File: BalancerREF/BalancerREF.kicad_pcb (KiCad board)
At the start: 2 copper layers, 69.8 x 54 mm, 101 parts, among them J1 USB4105-GF-A, J2 LiPo 500mAh PROTECTED, J3 MAG+ / MAG- PTH, J4 GPS MODULE 3V3 UART, Q1 AO3400A, Q3 AO3401A, Q4 AO3401A, SW1 POWER, SW2 ACQUIRE, SW3 BOOT / SERVICE, SW4 RESET, U1 ESP32-S3-MINI-1-N8, U10 SN74LVC1G123DCTR, U2 IIS3DWBTR, U3 LM1815MX/NOPB, U4 TS3021IYLT, U5 MCP73831T-2ACI/OT, U6 TPS63031DSKR, U7 SRV05-4MR6T1G, U8 TLV9062IDR, U9 SN74LVC1G08DBVR

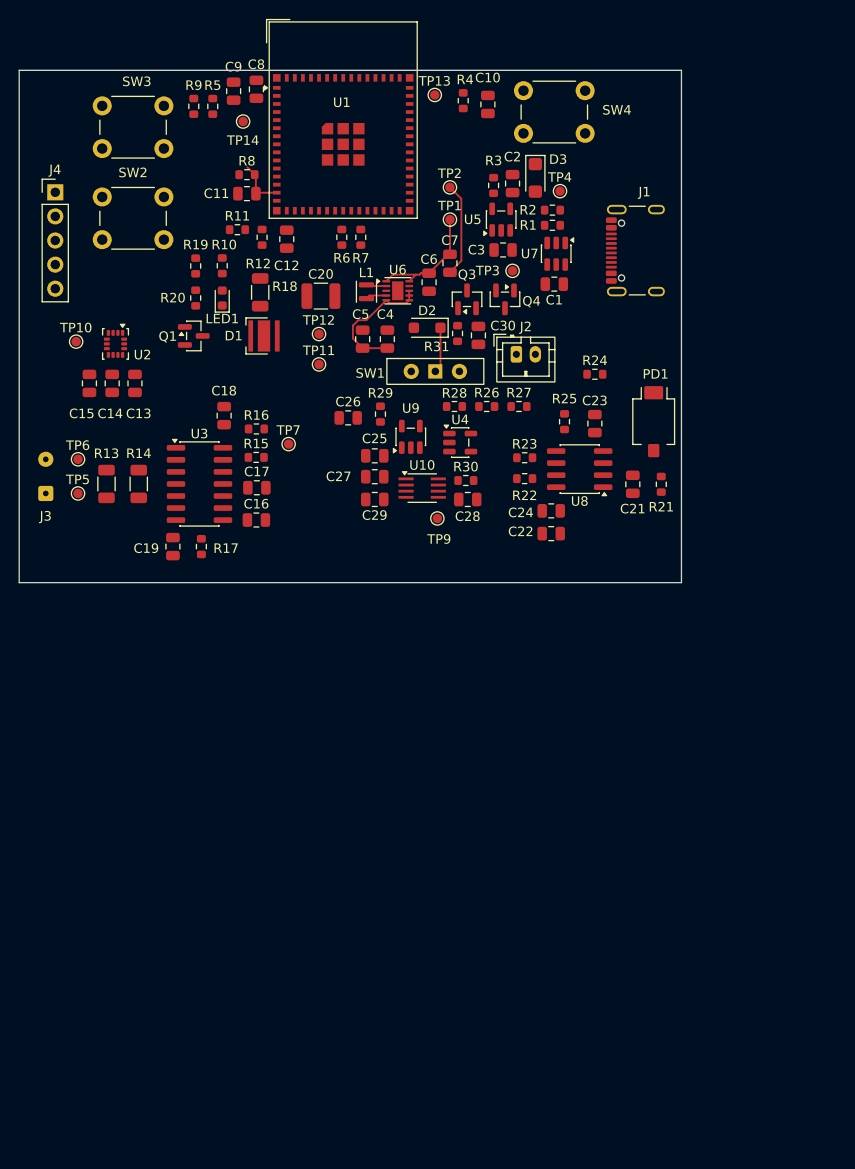
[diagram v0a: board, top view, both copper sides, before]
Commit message: feat: split optical head to its own board, place both PCBs
BalancerREF main board (50 x 50, 4 layer):
- optical front end removed to BalancerREF_OptHead; J5 7-way cable connector
  added, with ground interleaved between OPT_LED_EN and OPT_COMP
- SW4 (RESET) removed - SW1 feeds U6 VIN and EN, so the power slide already
  power-cycles the MCU; R4/C10/TP13 still hold EN high and probeable
- R5 removed - it duplicated R9's 10k BOOT pull-up on the same net
- all 83 footprints placed: ICs, connectors, switches and test points on the
  front, passives on the back under their own IC's power pins
- M2.5 mounting holes at the four corners
- UP / LEFT orientation markers on F.SilkS for vertical mounting with the
  ESP32 left and USB-C right
- DRC 2, both the U1 library courtyard overlapping the corner holes; U1's real
  antenna keepout is off-board thanks to the overhang

BalancerREF_OptHead (25 x 50, 2 layer), new PCB:
- every part on the front so B.Cu is an uninterrupted GND pour, which matters
  more than a clean optical face given the transimpedance summing node
- D1 centred on the optical axis, PD1 18 mm directly below, J5 on the bottom
- DRC 0

Verification:
- verify_netlist.py spec updated for the split and re-passing honestly. It had
  been reporting PASS against a stale netlist; regenerating that netlist made it
  crash, which is what the spec update fixes. PASS: 43 exact circuit nets,
  280 pin endpoints, 128 IC pads
- verify_head.py unchanged, PASS: 16 exact circuit nets, 63 pin endpoints
- review/ artifacts regenerated from the current schematic

Lens keepout radius and the D1-PD1 spacing are estimates pending the real
Ledil TINA holder dimensions.

Co-Authored-By: Claude Opus 5 (1M context) <noreply@anthropic.com>
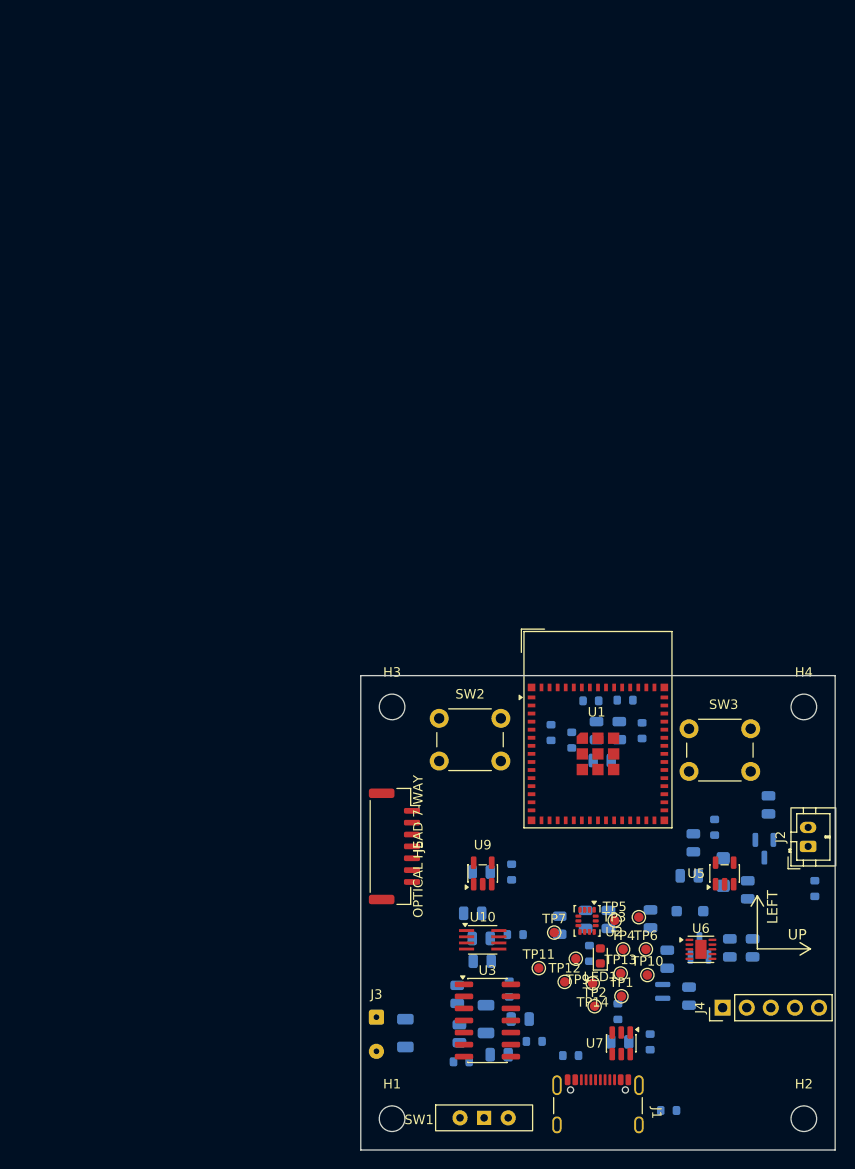
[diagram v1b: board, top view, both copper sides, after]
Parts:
- removed C20: 100u / 6.3V, Capacitor_SMD:C_1210_3225Metric
- removed C21: 10p C0G, Capacitor_SMD:C_0805_2012Metric
- removed C22: 10n, Capacitor_SMD:C_0805_2012Metric
- removed C23, C24, C25: 100n, Capacitor_SMD:C_0805_2012Metric
- removed D1: XPEBRD-L1 625nm, LED_SMD:LED_Cree-XP
- removed PD1: BPW34S, OptoDevice:Osram_BPW34S-SMD
- removed Q1: AO3400A, Package_TO_SOT_SMD:SOT-23
- removed R18: 3R0 1206 0.5W, Resistor_SMD:R_1206_3216Metric
- removed R19: 100R, Resistor_SMD:R_0603_1608Metric
- removed R20: 100k, Resistor_SMD:R_0603_1608Metric
- removed R21, R22, R24, R25, R27, R5: 10k, Resistor_SMD:R_0603_1608Metric
- removed R23: 120k, Resistor_SMD:R_0603_1608Metric
- removed R26: 22k, Resistor_SMD:R_0603_1608Metric
- removed R28: 470k, Resistor_SMD:R_0603_1608Metric
- removed SW4: RESET, Button_Switch_THT:SW_PUSH_6mm
- removed U4: TS3021IYLT, Package_TO_SOT_SMD:SOT-23-5
- removed U8: TLV9062IDR, Package_SO:SOIC-8_3.9x4.9mm_P1.27mm
- added H1: M2.5 MOUNT, MountingHole_2.7mm_M2.5, F.Cu at (103.3, 146.7)
- added H2: M2.5 MOUNT, MountingHole_2.7mm_M2.5, F.Cu at (146.7, 146.7)
- added H3: M2.5 MOUNT, MountingHole_2.7mm_M2.5, F.Cu at (103.3, 103.3)
- added H4: M2.5 MOUNT, MountingHole_2.7mm_M2.5, F.Cu at (146.7, 103.3)
- added J5: OPTICAL HEAD 7-WAY, Connector_JST:JST_GH_SM07B-GHS-TB_1x07-1MP_P1.25mm_Horizontal, F.Cu at (103.5, 118.0)
- C1, C10, C11, C12, C13, C14, C15, C16, C17, C18, C19, C2, C26, C27, C28, C29, C3, C30, C4, C5, C6, C7, C8, C9, D2, D3, L1, Q3, Q4, R1, R10, R11, R12, R13, R14, R15, R16, R17, R2, R29, R3, R30, R31, R4, R6, R7, R8, R9: moved to B.Cu
- moved J4 111.1 mm to (138.1, 135.0), turned to 90 degrees
- moved TP14 98.0 mm to (124.4, 132.4)
- moved TP13 94.6 mm to (127.4, 131.4)
- moved R1 94.1 mm to (132.4, 145.8), turned to 180 degrees
- moved J1 91.2 mm to (125.0, 146.3), turned to 0 degrees
- moved SW3 90.2 mm to (141.1, 110.1)
- moved R7 90.1 mm to (130.5, 138.6)
- moved TP10 89.9 mm to (130.2, 131.6)
- moved R2 89.1 mm to (122.1, 140.0), turned to 180 degrees
- moved C12 88.1 mm to (138.9, 128.7)
- moved TP2 87.6 mm to (124.7, 134.8)
- moved R6 86.6 mm to (127.1, 135.4)
- moved TP1 83.8 mm to (127.5, 133.8)
- moved U7 83.5 mm to (127.5, 138.8)
- moved R10 82.2 mm to (124.1, 129.3)
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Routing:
- net /SYS_SW: track 13.7 -> 0.00 mm
- net /+3V3: track 12.5 -> 0.00 mm
- net GND: track 9.94 -> 0.00 mm
- net /ACQUIRE_BUTTON: track 5.39 -> 0.00 mm
- net Net-(D2-K): track 4.82 -> 0.00 mm
- net Net-(U6-L1): track 2.22 -> 0.00 mm
- net Net-(U6-L2): track 2.14 -> 0.00 mm
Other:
- board size 69.8 x 54 mm -> 50 x 50 mm
- copper layers 2 -> 4
- board text added: "LEFT"
- board text added: "UP"

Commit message: feat: fiducials, net classes, and a BAT sense divider
Fiducials (1 mm dot / 2 mm mask), three per populated face at three of the
four corners - never four, since a symmetric set gives the placement machine
no way to distinguish a 180-degree-rotated panel. Main board gets both faces
(FID1-3 front, FID4-6 back); the optical head is single-sided so its back has
none.

Net classes set in both .kicad_pro, sized from IPC-2221 at 1 oz outer copper
and a 10 C rise (0.20 mm ~ 0.74 A, 0.50 ~ 1.45 A, 0.80 ~ 2.03 A):
  Default 0.20  Power 0.50  Switch 0.80 (main)  Emitter 0.80 (head)  USB pair
Switch clearance stays at 0.20 rather than 0.25: the TPS63031's WSON-10 puts
its own L1/L2 pads 0.20 mm from its thermal pad, so anything stricter fails
inside the package. The USB class exists for tuning and length matching but is
not an impedance solution - that needs the fab's stackup. The S3's native USB
is Full Speed, so it matters less than it would at High Speed.

BAT sense divider - R33/R34 (1M) and C31 (100n) on GPIO4 (ADC1_CH3):
SUPPLY_SENSE reads SYS_SW/2 and cannot separate USB from battery, because a
USB port at the low end of spec minus D2's drop lands near 4.30 V against a
full cell at 4.20 V - inside divider tolerance plus ADC error. Comparing
SYS_SW against BAT is a differential test and separates them cleanly. 1M/1M
rather than 100k/100k because this divider hangs on the cell even when the
puck is off (~2 uA vs ~21 uA); the resulting 500k source impedance means
firmware needs a long sample time and multisample.

U1 pin 8's no-connect removed and U1.8 dropped from unused-pins.json.

verify_netlist.py spec extended with BAT_SENSE and the new ground/BAT members.
  main PASS: 44 exact circuit nets, 286 pin endpoints, 128 IC pads
  head PASS: 16 exact circuit nets, 63 pin endpoints
ERC 0 errors. DRC: main 2 (U1 library courtyard vs the corner holes), head 0.
All 81 schematic parts confirmed present on the board; the only board-only
refs are the 6 fiducials and 4 mounting hole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
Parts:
- added C31: 100n, C_0805_2012Metric, B.Cu at (121.3, 111.4)
- added FID1: FIDUCIAL, Fiducial_1mm_Mask2mm, F.Cu at (141.5, 146.5)
- added FID2: FIDUCIAL, Fiducial_1mm_Mask2mm, F.Cu at (103.5, 127.0)
- added FID3: FIDUCIAL, Fiducial_1mm_Mask2mm, F.Cu at (142.5, 118.5)
- added FID4: FIDUCIAL, Fiducial_1mm_Mask2mm, B.Cu at (143.0, 146.5)
- added FID5: FIDUCIAL, Fiducial_1mm_Mask2mm, B.Cu at (103.5, 107.0)
- added FID6: FIDUCIAL, Fiducial_1mm_Mask2mm, B.Cu at (146.5, 107.0)
- added R33: 1M, R_0603_1608Metric, B.Cu at (117.8, 108.9)
- added R34: 1M, R_0603_1608Metric, B.Cu at (117.7, 110.9)

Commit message: feat: BQ24075 charge management, drop BAT_SENSE, sweep wire stubs
Replaces the MCP73831 + D2 + Q3 + R27 + R31 discrete charger and power-path
with a BQ24075RGT, which does the same job with an integrated DPPM path and
adds what the discrete version could not: independent system/charge supply,
operation with a defective or absent cell, USB-IF inrush limiting, and VIN-DPM
so a weak port sags instead of collapsing.

New support parts: R3 3.57k ISET (~249 mA, about 0.5C), R35 1.6k ILIM (~1.0 A),
R36 10k on TS for the absent pack thermistor, R37/R38 100k pull-ups, C30 10uF
on OUT. CE and SYSOFF tied low; TMR left open for the default safety timers.
EN1/EN2/PGOOD/CHG go to GPIO5/18/21/38.

BAT_SENSE (R33/R34/C31 on GPIO4) is removed. It existed only to infer USB
presence by comparing SYS_SW against BAT; PGOOD reports a valid input source
directly, so the inference is redundant. That also retires a 500k ADC source
impedance and a ~2uA standing drain on the cell.

Every BQ24075 pin is verified against SLUS810N Rev N, now saved in sources/.
Two things that check surfaced:
  - SYS sits ~0.4 V higher without D2's drop. Still inside the TPS63031's
    1.8-5.5 V recommended range, and the failure mode improved: OUT clamps at
    5.5 V and the input OVPs at 6.6 V, where the diode passed everything
    through. Wants a bench measurement with a 5.25 V source.
  - SUPPLY_SENSE is now the only supply measurement and it is on ADC2, the
    unit shared with the radio. That is why BAT_SENSE had been on ADC1.

Also in this change:
  - /SYS added to the Power net class. It is the BQ24075's OUT rail and
    carries the whole system load; at the 0.20 mm default it was rated 0.74 A.
    Dropped the dead Net-(D2-K) pattern.
  - Swept 19 dangling wire stubs plus an orphaned no-connect left by the
    optical split, SW4, R5 and this swap: 23 wires removed, 2 trimmed back to
    the label they carry. ERC goes from 20 warnings to 0.
  - Mounting holes pulled 0.25 mm inward so they clear U1's ante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
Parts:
- removed C31: 100n, C_0805_2012Metric
- removed D2: PMEG4010CEH, Diode_SMD:D_SOD-123F
- removed Q3: AO3401A, Package_TO_SOT_SMD:SOT-23
- removed R31: 1k, Resistor_SMD:R_0603_1608Metric
- removed R33, R34: 1M, R_0603_1608Metric
- added R35: 1.6k, R_0603_1608Metric, B.Cu at (136.9, 124.2)
- added R36: 10k, R_0603_1608Metric, B.Cu at (134.1, 114.4)
- added R37: 100k, R_0603_1608Metric, B.Cu at (137.6, 112.8)
- added R38: 100k, R_0603_1608Metric, B.Cu at (131.9, 118.3)
- R3: value 4.02k 1% -> 3.57k 1%
- U5: value MCP73831T-2ACI/OT -> BQ24075RGT; footprint Package_TO_SOT_SMD:SOT-23-5 -> QFN-16-1EP_3x3mm_P0.5mm_EP1.675x1.675mm
- moved U5 1.96 mm to (138.4, 118.9), turned to 0 degrees
- moved H1 0.25 mm to (103.3, 146.4)
- moved H2 0.25 mm to (146.7, 146.4)
- moved H3 0.25 mm to (103.3, 103.5)
- moved H4 0.25 mm to (146.7, 103.5)
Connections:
- C30 pad 1: Net-(D2-K) -> /SYS
- R3 pad 1: Net-(U5-PROG) -> /ISET
- SW1 pad 1: Net-(D2-K) -> /SYS
- U1 pad 22: unconnected-(U1-IO18-Pad22) -> /CHG_EN2
- U1 pad 25: unconnected-(U1-IO21-Pad25) -> /PGOOD_N
- U1 pad 34: unconnected-(U1-IO38-Pad34) -> /CHG_STAT
- U1 pad 9: unconnected-(U1-IO5-Pad9) -> /CHG_EN1
- U5 pad 1: unconnected-(U5-STAT-Pad1) -> /TS
- U5 pad 2: GND -> /BAT
- U5 pad 4: /USB_VBUS -> GND
- U5 pad 5: Net-(U5-PROG) -> /CHG_EN2
- U9 pad 1: Net-(R28-Pad1) -> /OPT_COMP

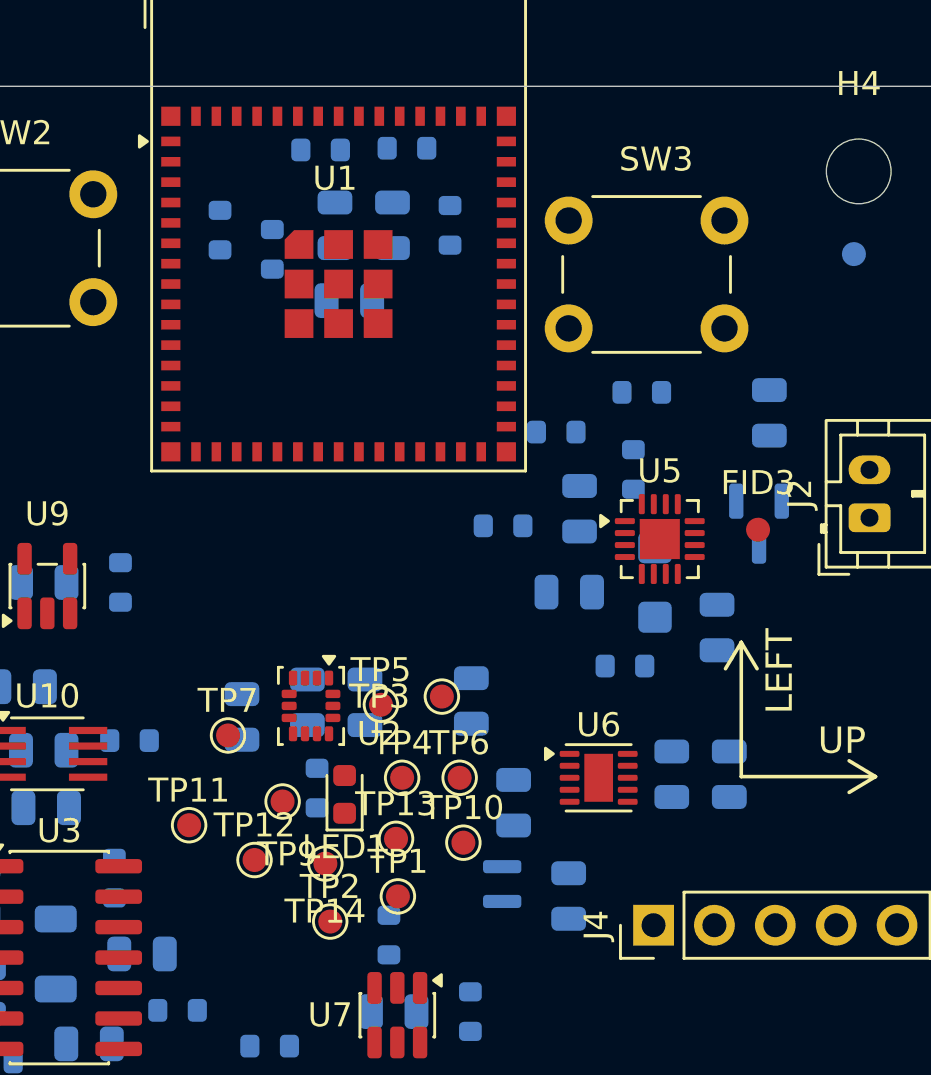
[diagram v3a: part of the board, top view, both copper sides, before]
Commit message: fix: address repo review findings before routing
An external review raised seven pre-routing items plus smaller notes. Each was
checked against the manufacturer source rather than taken on faith; two did not
survive that check and are recorded as not-confirmed.

Confirmed and fixed:

  * D1 peak current. The head runs from SYS_SW, and with the BQ24075 regulating
    OUT to 5.5 V, R18 at 3.0 ohm gave ~1.1 A peak against D1's 1 A absolute
    maximum. The BOM note had only checked the 4.2 V battery case, and the
    charger swap - which replaced a Schottky holding SYS near 4.55 V - is what
    pushed it over. R18 -> 3.9 ohm: ~0.49 A at a full cell (the bench-set design
    point) and ~0.90 A worst case at 5.5 V with a low-Vf bin.
  * Charger stuck at USB100. EN1/EN2 have 285k internal pulldowns and nothing
    drove them, so the input limit covered system load AND charge current at
    100 mA. setupCharger() now selects USB500 at boot, and status reports
    input_present/charging from PGOOD and CHG.
  * U9 input transition rate. R29/C26 fed the SN74LVC1G08 a 0.47 us edge against
    a 10 ns/V spec, ~25x out. Swapped to SN74LVC1G132, a Schmitt NAND with the
    identical SOT-23-5 pinout (verified against SLVS322 Figure 4-1), which
    conditions both inputs. It inverts, so U10's trigger moved from B rising to
    ~A falling - the SN74LVC1G123 supports both edges.
  * Switcher parts on the wrong face. L1 and C4-C7 were on the back with U6 on
    the front, putting vias in a 2.4 MHz switching loop. Moved to the front;
    C2/C3/C30 followed for the BQ24075. The "ICs front, passives back" rule does
    not survive contact with a switching converter.
  * U1 decoupling. C8 is now 0.38 mm from the 3V3 pad instead of ~9 mm. Both
    stay on the back, since U1's body owns that part of the front.
  * Head board emitter loop, was spanning the full board width. C20/R18/Q1 now
    cluster in 6.9 x 3.3 mm. R21/C21 went from 4 mm off Q1 to 16 mm and sit
    3.6/3.9 mm from U8 pins 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
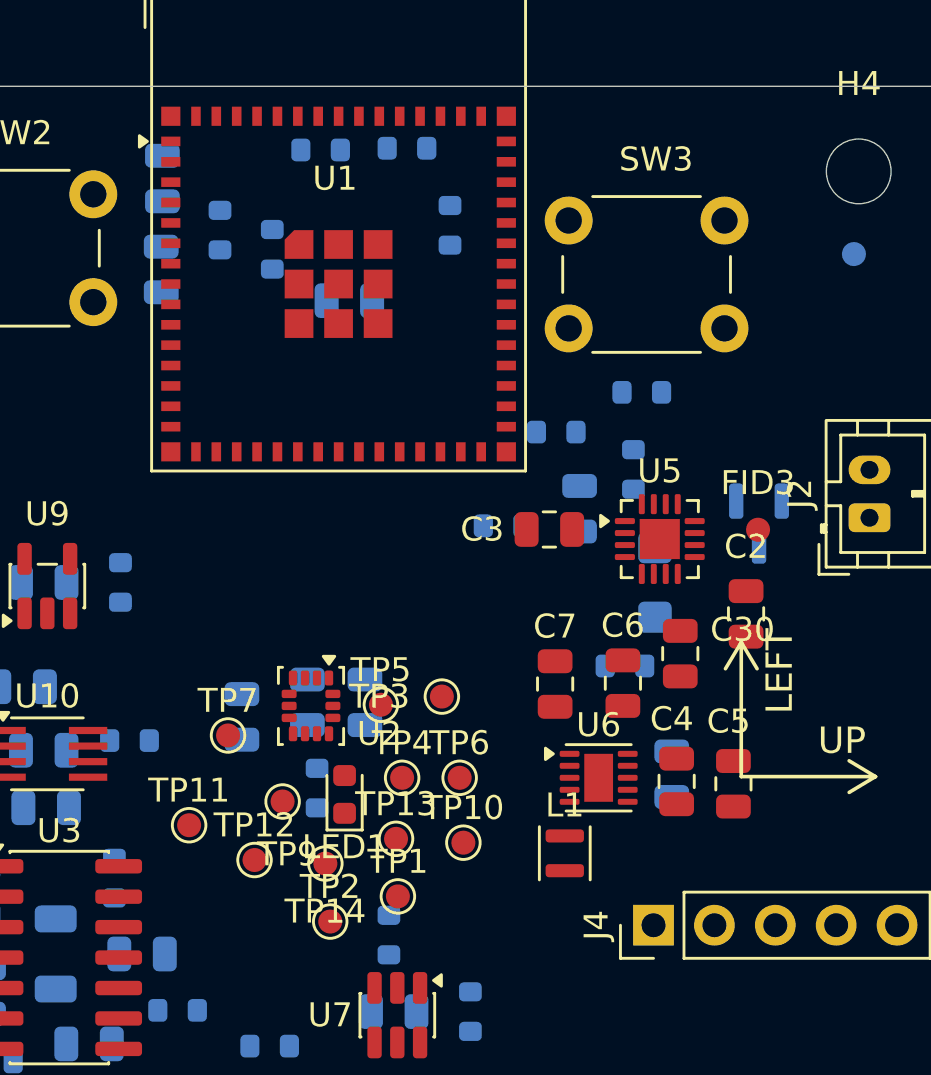
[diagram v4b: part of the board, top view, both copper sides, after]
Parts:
- C2, C3, C30, C4, C5, C6, C7, L1: moved to F.Cu
- U9: value SN74LVC1G08DBVR -> SN74LVC1G132DBVR
- moved C5 11.5 mm to (141.5, 129.1)
- moved C30 10.7 mm to (139.3, 123.7)
- moved C8 9.80 mm to (117.6, 103.8)
- moved C9 7.48 mm to (117.6, 107.6)
- moved C4 6.57 mm to (139.1, 129.0)
- moved C6 5.84 mm to (136.9, 124.9)
- moved C7 5.25 mm to (134.0, 124.9)
- moved L1 2.91 mm to (134.4, 132.0)
- moved C3 2.74 mm to (133.8, 118.5), turned to 180 degrees
- moved C2 1.34 mm to (142.0, 122.0)
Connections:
- U10 pad 1: GND -> Net-(U10-~{A})
- U10 pad 2: Net-(U10-B) -> /+3V3
- U9 pad 4: Net-(U10-B) -> Net-(U10-~{A})
